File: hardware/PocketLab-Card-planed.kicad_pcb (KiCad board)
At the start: 4 copper layers, 85.6 x 54 mm, 232 parts, among them J1 USB-C DATA/POWER, J2 microSD, J3 GNSS ANT U.FL, J4 PROTECTED 1S LiPo 3.7V, J5 2x15 2.54mm DUPONT EXPANSION, J7 OPTIONAL 10k NTC - CUT SJ1, Q1 AO3400A IR DRIVER, Q2 CSD16406Q3 DISCHARGE, Q3 CSD16406Q3 CHARGE, Q4 AO3400A BUZZER, SW1 RESET, SW2 BOOT, SW3 USER A, SW4 USER B, U1 ESP32-S3-WROOM-1-N8R2, U10 BMI270 (FULL OPTION), U11 BMP390 (FULL OPTION), U12 PCF8563T, U13 TSOP75338WTR 38kHz, U14 BQ29700DSE, U15 TPS2553DBVR 500mA LIMIT, U16 USBLC6-4SC6Y, U17 TPS22919DCKR GNSS LOAD SWITCH, U18 TCA9534PWR INTERNAL CONTROL, U19 SRV05-4MR6T1G SD ESD, U2 PN5321A3HN/C106, U3 E07-900M10S IPEX 868MHz, U4 MAX-M10S-00B, U5 BQ24074RGTR, U6 TPS63070RNMR 3V3, U7 TPS61023DRLR 5V BOOST, U8 MAX17048G+T10, U9 TCA9535PWR, Y301 27.12MHz crystal (pins 2/4 sh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, Y701 32.768kHz CL=7pF

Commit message: Save integrated card hardware and firmware checkpoint
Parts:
- removed BZ1: PKMCS0909E, Buzzer_Beeper:Buzzer_Murata_PKMCS0909E
- removed J7: OPTIONAL 10k NTC - CUT SJ1, Connector_PinHeader_2.54mm:PinHeader_1x02_P2.54mm_Vertical
- removed Q4: AO3400A BUZZER, Package_TO_SOT_SMD:SOT-23
- removed R607: 100k, Resistor_SMD:R_0805_2012Metric
- added A1: T3-868M SPRING ANTENNA, PocketLab_Custom:T3-868M_Edge_Solder, F.Cu at (86.8, 70.5)
- added C403: DNP SUBGHZ MATCH, Capacitor_SMD:C_0805_2012Metric, B.Cu at (75.4, 66.0)
- added C404: DNP SUBGHZ MATCH, Capacitor_SMD:C_0805_2012Metric, B.Cu at (82.8, 66.0)
- added C607: 22uF 10V X5R IR BUFFER, Capacitor_SMD:C_1206_3216Metric, F.Cu at (70.7, 61.5)
- added C608: 100nF IR HF, Capacitor_SMD:C_0805_2012Metric, F.Cu at (64.8, 68.5)
- added C609: 100nF X7R, Capacitor_SMD:C_0805_2012Metric, B.Cu at (65.5, 65.9)
- added C610: 1uF X7R, Capacitor_SMD:C_0805_2012Metric, F.Cu at (83.2, 54.5)
- added C611: 1uF X7R, Capacitor_SMD:C_0805_2012Metric, F.Cu at (83.2, 58.3)
- added C612: 100nF X7R, Capacitor_SMD:C_0805_2012Metric, F.Cu at (80.8, 54.5)
- added C613: 4.7uF X5R, Capacitor_SMD:C_0805_2012Metric, F.Cu at (80.8, 58.3)
- added C614: 2.2uF X7R, Capacitor_SMD:C_0805_2012Metric, F.Cu at (83.2, 62.0)
- added C615: 4.7uF X5R, Capacitor_SMD:C_0805_2012Metric, F.Cu at (80.8, 62.0)
- added C616: 100nF X7R, Capacitor_SMD:C_0805_2012Metric, B.Cu at (81.0, 62.2)
- added C617: 22uF 10V X5R IR BUFFER, Capacitor_SMD:C_1206_3216Metric, B.Cu at (65.0, 62.1)
- added D2: TSAL6200 940nm, PocketLab_Custom:TSAL6200_LayFlat_Inboard, F.Cu at (20.2, 62.2)
- added D3: TSAL6200 940nm, PocketLab_Custom:TSAL6200_LayFlat_Inboard, F.Cu at (20.2, 68.6)
- added J8: ER-OLED0.42-1W 72x40 SSD1306B, PocketLab_Custom:EastRising_ER-OLED0.42-1W_SolderFPC, F.Cu at (90.5, 58.5)
- added J9: GPIO38 2.54mm DUPONT, Connector_PinHeader_2.54mm:PinHeader_1x01_P2.54mm_Vertical, F.Cu at (102.7, 69.5)
- added R405: 0R SUBGHZ MATCH, Resistor_SMD:R_0805_2012Metric, B.Cu at (79.1, 66.0)
- added R610: 39R 0.5W pulse-rated, Resistor_SMD:R_1210_3225Metric, B.Cu at (40.8, 61.8)
- added R611: 39R 0.5W pulse-rated, Resistor_SMD:R_1210_3225Metric, B.Cu at (46.9, 57.5)
- added R735: 100k EN pull-down, Resistor_SMD:R_0805_2012Metric, B.Cu at (85.7, 31.8)
- added SW5: MAIN POWER OFF / ON, Button_Switch_SMD:SW_SPDT_Shouhan_MSK12C02, F.Cu at (92.9, 69.3)
- added U20: SN74AHCT1G126DBVR RGB LEVEL SHIFT, Package_TO_SOT_SMD:SOT-23-5, F.Cu at (65.8, 60.8)
- C501, C502, C603, C604, C605, C606, D501, J3, J4, R501, R502, R505, R608, R609, R710, R711, R712, R715, TP502, TP601: moved to B.Cu
- C510, C511, R401, R402, R403, R404, R510, R511, R512, R513, R730, R731, R732, R733, U19: moved to F.Cu
- D1: footprint LED_THT:LED_D5.0mm -> PocketLab_Custom:TSAL6200_LayFlat_Inboard
- J5: value 2x15 2.54mm DUPONT EXPANSION -> 30-PIN 2.54mm DUPONT GRID; footprint Connector_PinHeader_2.54mm:PinHeader_2x15_P2.54mm_Vertical -> PocketLab_Custom:Dupont_Grid_6x5_P2.54mm
- LED1, LED2, LED3: value WS2812B-MINI-V3 -> WS2812B-2020; footprint LED_SMD:LED_WS2812B-Mini_PLCC4_3.5x3.5mm -> LED_SMD:LED_WS2812B-2020_PLCC4_2.0x2.0mm
- LED4: value WS2812B-MINI-V3 -> WS2812B-2020; footprint LED_SMD:LED_WS2812B-Mini_PLCC4_3.5x3.5mm -> LED_SMD:LED_WS2812B-2020_PLCC4_2.0x2.0mm; moved to F.Cu
- Q2, Q3: footprint Package_SON:VSON-8_3.3x3.3mm_P0.65mm_NexFET -> PocketLab_Custom:CSD16406Q3_VSON-8_3.3x3.3mm_P0.65mm_JLC
- R601: value 39R 1W pulse-rated -> 39R 0.5W pulse-rated; footprint Resistor_SMD:R_2512_6332Metric -> Resistor_SMD:R_1210_3225Metric
- R605: value 330R -> 68R; moved to B.Cu
- R606: value 100R -> 100R GPIO38 PROTECTION; moved to B.Cu
- SW1: footprint Button_Switch_SMD:SW_SPST_TL3305A -> Button_Switch_SMD:SW_Push_1P1T_NO_CK_KMR2
- SW2: footprint Button_Switch_SMD:SW_SPST_TL3305A -> Button_Switch_SMD:SW_Push_1P1T_NO_CK_KMR2; moved to F.Cu
- U1: footprint RF_Module:ESP32-S3-WROOM-1 -> PocketLab_Card:ESP32-S3-WROOM-1_PhysicalCourtyard
- U3: value E07-900M10S IPEX 868MHz -> E07-900MM10S 855-925MHz; footprint PocketLab_Custom:E07-900M10S -> PocketLab_Custom:E07-900MM10S
- moved R128 75.2 mm to (90.6, 32.0)
- moved R513 67.1 mm to (103.1, 42.5), turned to 90 degrees
- moved C605 66.9 mm to (25.7, 21.8), turned to 180 degrees
- moved C606 66.9 mm to (29.7, 21.8), turned to 180 degrees
- moved TP101 66.7 mm to (25.5, 22.3)
- moved U19 66.6 mm to (103.8, 38.5), turned to 90 degrees
- moved TP102 65.8 mm to (28.0, 22.3)
- moved U12 65.5 mm to (42.0, 69.5), turned to 0 degrees
- moved R731 59.6 mm to (82.2, 65.3), turned to 0 degrees
- moved R127 58.6 mm to (90.7, 59.2)
- moved R511 57.2 mm to (87.2, 51.4)
- moved D1 57.1 mm to (20.2, 55.8), turned to 0 degrees
- moved R510 57.0 mm to (81.5, 38.9)
- moved Y701 56.5 mm to (35.5, 69.5), turned to -90 degrees
- moved R605 56.0 mm to (33.7, 21.8), turned to 180 degrees
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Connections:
- net +5V_AUX renamed /+5V_AUX
- net AUX5_EN renamed /AUX5_EN
- net AUX5_FAULT_N renamed /AUX5_FAULT_N
- net BAT_COUT renamed /BAT_COUT
- net BAT_DOUT renamed /BAT_DOUT
- net BAT_FET_MID renamed /BAT_FET_MID
- net BAT_SENSE renamed /BAT_SENSE
- net BAT_VMINUS renamed /BAT_VMINUS
- net BMI_INT1 renamed /BMI_INT1
- net BMI_INT2 renamed /BMI_INT2
- net BMP_INT renamed /BMP_INT
- net BOOST5_EN renamed /BOOST5_EN
- net BOOT_N renamed /BOOT_N
- net BQ_EN1 renamed /BQ_EN1
- net BQ_EN2 renamed /BQ_EN2
- net BUZZER_PWM renamed /GPIO38_MCU
- net CELL_NEG renamed /CELL_NEG
- net CELL_POS renamed /CELL_POS
- net CHARGER_CHG_N renamed /CHARGER_CHG_N
- net CHARGER_PGOOD_N renamed /CHARGER_PGOOD_N
- net CHG_DISABLE renamed /CHG_DISABLE
- net CHG_ILIM renamed /CHG_ILIM
- net CHG_ISET renamed /CHG_ISET
- net CHG_ITERM renamed /CHG_ITERM
- net CHG_TMR renamed /CHG_TMR
- net CHG_TS_FIXED renamed /CHG_TS_FIXED
- net ESP_EN renamed /ESP_EN
- net EX0 renamed /EX0
- net EX0_INT renamed /EX0_INT
- net EX1 renamed /EX1
- net EX1_INT renamed /EX1_INT
- net EX2 renamed /EX2
- net EX2_INT renamed /EX2_INT
- net EX3 renamed /EX3
- net EX3_INT renamed /EX3_INT
- net EX4 renamed /EX4
- net EX4_INT renamed /EX4_INT
- net EX5 renamed /EX5
- net EX5_INT renamed /EX5_INT
- net EX6 renamed /EX6
- net EX6_INT renamed /EX6_INT
- net EX7 renamed /EX7
- net EX7_INT renamed /EX7_INT
- net FG_ALERT_N renamed /FG_ALERT_N
- net GNSS_3V3 renamed /GNSS_3V3
- net GNSS_ANT_FEED renamed /GNSS_ANT_FEED
- net GNSS_BIAS renamed /GNSS_BIAS
- net GNSS_LNA_EN renamed /GNSS_LNA_EN
- net GNSS_POWER_EN renamed /GNSS_POWER_EN
- net GNSS_QOD renamed /GNSS_QOD
- net GNSS_RESET_N renamed /GNSS_RESET_N
- net GNSS_RX_FROM_MODULE renamed /GNSS_RX_FROM_MODULE
- net GNSS_TIMEPULSE renamed /GNSS_TIMEPULSE
- net GNSS_TX_TO_MODULE renamed /GNSS_TX_TO_MODULE
- net GNSS_UART_RX_MOD renamed /GNSS_UART_RX_MOD
- net GNSS_UART_TX_MOD renamed /GNSS_UART_TX_MOD
- net GNSS_VCC_RF renamed /GNSS_VCC_RF
- net GPIO1 renamed /GPIO1
- net GPIO1_MCU renamed /GPIO1_MCU
- net GPIO2 renamed /GPIO2
- net GPIO2_MCU renamed /GPIO2_MCU
- net GPIO4 renamed /GPIO4
- net GPIO40 renamed /GPIO40
- net GPIO40_MCU renamed /GPIO40_MCU
- net GPIO41 renamed /GPIO41
- net GPIO41_MCU renamed /GPIO41_MCU
- net GPIO42 renamed /GPIO42
- net GPIO42_MCU renamed /GPIO42_MCU
- net GPIO43 renamed /GPIO43
- net GPIO43_MCU renamed /GPIO43_MCU
- net GPIO44 renamed /GPIO44
- net GPIO44_MCU renamed /GPIO44_MCU
- net GPIO47 renamed /GPIO47
- net GPIO47_MCU renamed /GPIO47_MCU
- net GPIO48 renamed /GPIO48
- net GPIO48_MCU renamed /GPIO48_MCU
- net GPIO4_MCU renamed /GPIO4_MCU
- net GPIO8 renamed /GPIO8
- net GPIO8_MCU renamed /GPIO8_MCU
- net GPIO9 renamed /GPIO9
- net GPIO9_MCU renamed /GPIO9_MCU
- net I2C_SCL renamed /I2C_SCL
- net I2C_SCL_HDR renamed /I2C_SCL_HDR
- net I2C_SDA renamed /I2C_SDA
- net I2C_SDA_HDR renamed /I2C_SDA_HDR
- net IOEXP_INT_N renamed /IOEXP_INT_N
- net IR_GATE renamed /IR_GATE
- net IR_LED_A renamed /IR_LED_A1
- net IR_LED_K renamed /IR_LED_K
- net IR_RX renamed /IR_RX
- net IR_RX_VS renamed /IR_RX_VS
- net IR_TX renamed /IR_TX
- net JTAG_STRAP_TP renamed /JTAG_STRAP_TP
- net NFC_DVDD renamed /NFC_DVDD
- net NFC_I0 renamed /NFC_I0
- net NFC_IRQ_N renamed /NFC_IRQ_N
- net NFC_LOADMOD renamed /NFC_LOADMOD
- net NFC_LOOP_A renamed /NFC_LOOP_A
- net NFC_LOOP_B renamed /NFC_LOOP_B
- net NFC_OSCIN renamed /NFC_OSCIN
- net NFC_OSCOUT renamed /NFC_OSCOUT
- net NFC_RESET_N renamed /NFC_RESET_N
- net NFC_RX renamed /NFC_RX
- net NFC_RX_AC renamed /NFC_RX_AC
- net NFC_SVDD renamed /NFC_SVDD
- net NFC_TX1 renamed /NFC_TX1
- net NFC_TX1_F renamed /NFC_TX1_F
- net NFC_TX2 renamed /NFC_TX2
- net NFC_TX2_F renamed /NFC_TX2_F
- net NFC_VMID renamed /NFC_VMID
- net PWR_3V3_PG renamed /PWR_3V3_PG
- net RGB_D1_2 renamed /RGB_D1_2
- net RGB_D2_3 renamed /RGB_D2_3
- net RGB_D3_4 renamed /RGB_D3_4
- net RGB_DIN1 renamed /RGB_DIN1
- net RGB_DOUT4 renamed /RGB_DOUT4
- net RTC_OSCI renamed /RTC_OSCI
- net RTC_OSCO renamed /RTC_OSCO
- net SD_CS_DEV renamed /SD_CS_DEV
- net SD_CS_N renamed /SD_CS_N
- net SD_DAT1 renamed /SD_DAT1
- net SD_DAT2 renamed /SD_DAT2
- net SD_DETECT_N renamed /SD_DETECT_N
- net SD_MISO renamed /SD_MISO
- net SD_MOSI renamed /SD_MOSI
- net SD_SCK renamed /SD_SCK
- net SPI_MISO renamed /SPI_MISO
- net SPI_MISO_HDR renamed /SPI_MISO_HDR
- net SPI_MOSI renamed /SPI_MOSI
- net SPI_MOSI_HDR renamed /SPI_MOSI_HDR
- net SPI_SCK renamed /SPI_SCK
- net SPI_SCK_HDR renamed /SPI_SCK_HDR
- net STRAP_BOOT_TP renamed /STRAP_BOOT_TP
- net STRAP_VDD_SPI_TP renamed /STRAP_VDD_SPI_TP
- net SUBGHZ_CS_N renamed /SUBGHZ_CS_N
- net U15_ILIM renamed /U15_ILIM
- net U6_FB renamed /U6_FB
- net U6_L1 renamed /U6_L1
- net U6_L2 renamed /U6_L2
- net U6_VAUX renamed /U6_VAUX
- net U7_FB renamed /U7_FB
- net U7_SW renamed /U7_SW
- net USB_CC1 renamed /USB_CC1
- net USB_CC2 renamed /USB_CC2
- net USB_CONN_N renamed /USB_CONN_N
- net USB_CONN_P renamed /USB_CONN_P
- net USB_D_N renamed /USB_D_N
- net USB_D_P renamed /USB_D_P
- net USB_SHIELD renamed /USB_SHIELD
- net USER_BUTTON_A_N renamed /USER_BUTTON_A_N
- net USER_BUTTON_B_N renamed /USER_BUTTON_B_N
- net VBUS_FUSED renamed /VBUS_FUSED
- net VBUS_USB renamed /VBUS_USB
- C101 pad 2: GND -> /GND
- C103 pad 2: GND -> /GND
- C104 pad 2: GND -> /GND
- C105 pad 1: VSYS -> /VSYS
- C105 pad 2: GND -> /GND
- C106 pad 2: GND -> /GND
- C107 pad 2: GND -> /GND
- C108 pad 1: VSYS -> /VSYS
- C108 pad 2: GND -> /GND
- C109 pad 1: VSYS -> /VSYS
- C109 pad 2: GND -> /GND
- C110 pad 1: +3V3 -> /+3V3
- C110 pad 2: GND -> /GND
- C111 pad 1: +3V3 -> /+3V3
- C111 pad 2: GND -> /GND
- C112 pad 1: +3V3 -> /+3V3
- C112 pad 2: GND -> /GND
- C113 pad 1: +5V_RAW -> /+5V_RAW
- C114 pad 1: VSYS -> /VSYS
- C114 pad 2: GND -> /GND
- C115 pad 1: +5V_RAW -> /+5V_RAW
- C115 pad 2: GND -> /GND
- C116 pad 1: +5V_RAW -> /+5V_RAW
- C116 pad 2: GND -> /GND
- C117 pad 1: +5V_RAW -> /+5V_RAW
- C117 pad 2: GND -> /GND
- C118 pad 2: GND -> /GND
- C119 pad 2: GND -> /GND
- C120 pad 2: GND -> /GND
- C121 pad 2: GND -> /GND
- C122 pad 1: VSYS -> /VSYS
- C122 pad 2: GND -> /GND
- C123 pad 1: VSYS -> /VSYS
- C123 pad 2: GND -> /GND
- C124 pad 1: +3V3 -> /+3V3
- C124 pad 2: GND -> /GND
- C201 pad 2: GND -> /GND
- C202 pad 1: +3V3 -> /+3V3
- C202 pad 2: GND -> /GND
- C203 pad 1: +3V3 -> /+3V3
- C203 pad 2: GND -> /GND
- C301 pad 2: GND -> /GND
- C302 pad 2: GND -> /GND
- C303 pad 1: +3V3 -> /+3V3
- C303 pad 2: GND -> /GND
- C304 pad 2: GND -> /GND
- C305 pad 2: GND -> /GND
- C306 pad 2: GND -> /GND
- C307 pad 2: GND -> /GND
- C308 pad 2: GND -> /GND
- C309 pad 2: GND -> /GND
- C311 pad 2: GND -> /GND
- C312 pad 2: GND -> /GND
- C313 pad 2: GND -> /GND
- C314 pad 2: GND -> /GND
- C315 pad 2: GND -> /GND
- C316 pad 1: +3V3 -> /+3V3
- C316 pad 2: GND -> /GND
- C317 pad 1: +3V3 -> /+3V3
- C317 pad 2: GND -> /GND
- C401 pad 1: +3V3 -> /+3V3
- C401 pad 2: GND -> /GND
- C402 pad 1: +3V3 -> /+3V3
- C402 pad 2: GND -> /GND
- C501 pad 2: GND -> /GND
- C502 pad 2: GND -> /GND
- C504 pad 2: GND -> /GND
- C510 pad 1: +3V3 -> /+3V3
- C510 pad 2: GND -> /GND
- C511 pad 1: +3V3 -> /+3V3
- C511 pad 2: GND -> /GND
- C512 pad 1: +3V3 -> /+3V3
- C512 pad 2: GND -> /GND
- C601 pad 2: GND -> /GND
- C602 pad 2: GND -> /GND
- C603 pad 1: +3V3 -> /+5V_RAW
- C603 pad 2: GND -> /GND
- C604 pad 1: +3V3 -> /+5V_RAW
- C604 pad 2: GND -> /GND
- C605 pad 1: +3V3 -> /+5V_RAW
- C605 pad 2: GND -> /GND
- C606 pad 1: +3V3 -> /+5V_RAW
- C606 pad 2: GND -> /GND
- C701 pad 1: +3V3 -> /+3V3
- C701 pad 2: GND -> /GND
- C702 pad 1: +3V3 -> /+3V3
- C702 pad 2: GND -> /GND
- C703 pad 1: +3V3 -> /+3V3
- C703 pad 2: GND -> /GND
- C704 pad 1: +3V3 -> /+3V3
- C704 pad 2: GND -> /GND
- C705 pad 1: +3V3 -> /+3V3
- C705 pad 2: GND -> /GND
- C706 pad 1: +3V3 -> /+3V3
- C706 pad 2: GND -> /GND
- C707 pad 1: +3V3 -> /+3V3
- C707 pad 2: GND -> /GND
- D101 pad 2: GND -> /GND
- D501 pad 1: GND -> /GND
- J1 pad A1: GND -> /GND
- J1 pad A12: GND -> /GND
- J1 pad B1: GND -> /GND
- J1 pad B12: GND -> /GND
- J2 pad 4: +3V3 -> /+3V3
- J2 pad 6: GND -> /GND
- J2 pad 9: GND -> /GND
- J2 pad SH: GND -> /GND
- J3 pad 2: GND -> /GND
- J5 pad 1: +3V3 -> /+3V3
- J5 pad 2: GND -> /GND
- J5 pad 28: GND -> /CHG_TS
- J5 pad 30: GND -> /GND
- L7 pad 1: VSYS -> /VSYS
- LED1 pad 1: +3V3 -> /+5V_RAW
- LED1 pad 3: GND -> /GND
- LED2 pad 1: +3V3 -> /+5V_RAW
- LED2 pad 3: GND -> /GND
- LED3 pad 1: +3V3 -> /+5V_RAW
- LED3 pad 3: GND -> /GND
- LED4 pad 1: +3V3 -> /+5V_RAW
- LED4 pad 3: GND -> /GND
- Q1 pad 2: GND -> /GND
- Q3 pad 1: GND -> /GND
- Q3 pad 2: GND -> /GND
- Q3 pad 3: GND -> /GND
- R101 pad 2: GND -> /GND
- R102 pad 2: GND -> /GND
- R103 pad 2: GND -> /GND
- R105 pad 2: GND -> /GND
- R107 pad 2: GND -> /GND
- R108 pad 2: GND -> /GND
- R109 pad 2: +3V3 -> /+3V3
- R110 pad 2: +3V3 -> /+3V3
- R111 pad 2: GND -> /GND
- R112 pad 2: GND -> /GND
- R113 pad 2: GND -> /GND
- R114 pad 2: GND -> /GND
- R115 pad 2: GND -> /GND
- R116 pad 1: VSYS -> /VSYS
- R116 pad 2: U6_PS_SYNC -> /PWR_SW_ON
- R117 pad 1: +3V3 -> /+3V3
- R118 pad 2: GND -> /GND
- R119 pad 2: +3V3 -> /+3V3
- R120 pad 1: +5V_RAW -> /+5V_RAW
- R121 pad 2: GND -> /GND
- R122 pad 2: GND -> /GND
- R123 pad 2: GND -> /GND
- R124 pad 2: +3V3 -> /+3V3
- R125 pad 2: +3V3 -> /+3V3
- R126 pad 2: GND -> /GND
- R127 pad 2: GND -> /GND
- R128 pad 2: GND -> /GND
- R203 pad 2: +3V3 -> /+3V3
- R204 pad 2: +3V3 -> /+3V3
- R302 pad 2: GND -> /GND
- R401 pad 2: SUB_SCK -> /SUB_SCK
- R402 pad 2: SUB_MOSI -> /SUB_MOSI
- R403 pad 2: SUB_MISO -> /SUB_MISO
- R404 pad 2: SUB_CS_N -> /SUB_CS_N
- R406 pad 1: SUB_CS_N -> /SUB_CS_N
- R406 pad 2: +3V3 -> /+3V3
- R506 pad 2: GND -> /GND
- R514 pad 2: +3V3 -> /+3V3
- R515 pad 2: +3V3 -> /+3V3
- R516 pad 2: +3V3 -> /+3V3
- R517 pad 2: +3V3 -> /+3V3
- R518 pad 2: +3V3 -> /+3V3
- R519 pad 2: +3V3 -> /+3V3
- R601 pad 1: +5V_RAW -> /+5V_RAW
- R603 pad 2: GND -> /GND
- R604 pad 1: +3V3 -> /+3V3
- R605 pad 1: RGB_DATA -> /RGB_BUF_5V
- R606 pad 2: BUZZER_GATE -> /GPIO38
- R608 pad 2: +3V3 -> /+3V3
- R609 pad 2: +3V3 -> /+3V3
- R701 pad 2: +3V3 -> /+3V3
- R702 pad 2: +3V3 -> /+3V3
- R703 pad 2: +3V3 -> /+3V3
- SJ1 pad 1: CHG_TS -> /CHG_TS
- SW1 pad 2: GND -> /GND
- SW2 pad 2: GND -> /GND
- SW3 pad 2: GND -> /GND
- SW4 pad 2: GND -> /GND
- TP104 pad 1: GND -> /GND
- TP107 pad 1: VSYS -> /VSYS
- TP108 pad 1: +3V3 -> /+3V3
- TP109 pad 1: +5V_RAW -> /+5V_RAW
- U1 pad 1: GND -> /GND
- U1 pad 18: RGB_DATA -> /RGB_DATA
- U1 pad 2: +3V3 -> /+3V3
- U1 pad 40: GND -> /GND
- U1 pad 41: GND -> /GND
- U1 pad 8: SUBGHZ_GDO0 -> /SUBGHZ_GDO0
- U1 pad 9: SUBGHZ_GDO2 -> /SUBGHZ_GDO2
- U10 pad 1: GND -> /GND
- U10 pad 10: (no net) -> unconnected-(U10-Pin_10-Pad10)
- U10 pad 11: (no net) -> unconnected-(U10-Pin_11-Pad11)
- U10 pad 12: +3V3 -> /+3V3
- U10 pad 2: (no net) -> unconnected-(U10-Pin_2-Pad2)
- U10 pad 3: (no net) -> unconnected-(U10-Pin_3-Pad3)
- U10 pad 5: +3V3 -> /+3V3
- U10 pad 6: GND -> /GND
- U10 pad 7: GND -> /GND
- U10 pad 8: +3V3 -> /+3V3
- U11 pad 1: +3V3 -> /+3V3
- U11 pad 10: +3V3 -> /+3V3
- U11 pad 3: GND -> /GND
- U11 pad 5: GND -> /GND
- U11 pad 6: +3V3 -> /+3V3
- U11 pad 8: GND -> /GND
- U11 pad 9: GND -> /GND
- U12 pad 3: (no net) -> unconnected-(U12-~{INT}-Pad3)
- U12 pad 4: GND -> /GND
- U12 pad 7: (no net) -> unconnected-(U12-CLKO-Pad7)
- U12 pad 8: +3V3 -> /+3V3
- U13 pad 1: GND -> /GND
- U13 pad 4: GND -> /GND
- U14 pad 1: (no net) -> unconnected-(U14-NC-Pad1)
- U15 pad 1: +5V_RAW -> /+5V_RAW
- U15 pad 2: GND -> /GND
- U16 pad 2: GND -> /GND
- U17 pad 1: +3V3 -> /+3V3
- U17 pad 2: GND -> /GND
- U17 pad 4: (no net) -> unconnected-(U17-Pin_4-Pad4)
- U18 pad 1: +3V3 -> /+3V3
- U18 pad 16: +3V3 -> /+3V3
- U18 pad 2: GND -> /GND
- U18 pad 3: GND -> /GND
- U18 pad 8: GND -> /GND
- U19 pad 2: GND -> /GND
- U19 pad 5: +3V3 -> /+3V3
- U2 pad 1: GND -> /GND
- U2 pad 11: GND -> /GND
- U2 pad 12: (no net) -> unconnected-(U2-AUX1-Pad12)
- U2 pad 13: (no net) -> unconnected-(U2-AUX2-Pad13)
- U2 pad 17: GND -> /GND
- U2 pad 18: GND -> /GND
- U2 pad 19: (no net) -> unconnected-(U2-P35-Pad19)
- U2 pad 20: (no net) -> unconnected-(U2-N.C.-Pad20)
- U2 pad 21: (no net) -> unconnected-(U2-N.C.-Pad21)
- U2 pad 22: (no net) -> unconnected-(U2-N.C.-Pad22)
- U2 pad 23: +3V3 -> /+3V3
- U2 pad 24: (no net) -> unconnected-(U2-P30/UART_RX-Pad24)
- U2 pad 26: (no net) -> unconnected-(U2-~{RSTOUT}-Pad26)
- U2 pad 29: (no net) -> unconnected-(U2-MISO/P71-Pad29)
- U2 pad 3: GND -> /GND
- U2 pad 30: (no net) -> unconnected-(U2-SCK/P72-Pad30)
- U2 pad 31: (no net) -> unconnected-(U2-P31/UART_TX-Pad31)
- U2 pad 32: (no net) -> unconnected-(U2-P32_INT0-Pad32)
- U2 pad 33: (no net) -> unconnected-(U2-P33_INT1-Pad33)
- U2 pad 34: (no net) -> unconnected-(U2-SIC_CLK/P34-Pad34)
- U2 pad 35: (no net) -> unconnected-(U2-SIGOUT-Pad35)
- U2 pad 36: (no net) -> unconnected-(U2-SIGIN-Pad36)
- U2 pad 40: +3V3 -> /+3V3
- U2 pad 41: GND -> /GND
- U2 pad 7: GND -> /GND
- U3 pad 1: GND -> /+3V3
- U3 pad 10: (no net) -> unconnected-(U3-Pin_10-Pad10)
- U3 pad 11: GND -> unconnected-(U3-Pin_11-Pad11)
- U3 pad 12: GND -> /SUB_MISO
- U3 pad 13: (no net) -> /SUB_MOSI
- U3 pad 14: SUBGHZ_GDO2 -> /SUB_CS_N
- U3 pad 15: SUBGHZ_GDO0 -> /SUB_SCK
- U3 pad 16: SUB_MISO -> /GND
- U3 pad 17: SUB_MOSI -> unconnected-(U3-Pin_17-Pad17)
- U3 pad 18: SUB_SCK -> /SUBGHZ_GDO0
- U3 pad 19: SUB_CS_N -> unconnected-(U3-Pin_19-Pad19)
- U3 pad 2: GND -> /GND
- U3 pad 20: GND -> /SUBGHZ_GDO2
- U3 pad 3: GND -> unconnected-(U3-Pin_3-Pad3)
- U3 pad 4: GND -> unconnected-(U3-Pin_4-Pad4)
- U3 pad 5: GND -> unconnected-(U3-Pin_5-Pad5)
- U3 pad 6: (no net) -> /SUBGHZ_RF_MOD
- U3 pad 7: (no net) -> /GND
- U3 pad 8: (no net) -> unconnected-(U3-Pin_8-Pad8)
- U3 pad 9: +3V3 -> unconnected-(U3-Pin_9-Pad9)
- U4 pad 1: GND -> /GND
- U4 pad 10: GND -> /GND
- U4 pad 12: GND -> /GND
- U4 pad 15: (no net) -> unconnected-(U4-VIO_SEL-Pad15)
- U4 pad 16: (no net) -> unconnected-(U4-SDA-Pad16)
- U4 pad 17: (no net) -> unconnected-(U4-SCL-Pad17)
- U4 pad 18: (no net) -> unconnected-(U4-~{SAFEBOOT}-Pad18)
- U4 pad 5: (no net) -> unconnected-(U4-EXTINT-Pad5)
- U4 pad 6: (no net) -> unconnected-(U4-V_BCKP-Pad6)
- U5 pad 1: CHG_TS -> /CHG_TS
- U5 pad 10: VSYS -> /VSYS
- U5 pad 11: VSYS -> /VSYS
- U5 pad 17: GND -> /GND
- U5 pad 8: GND -> /GND
- U6 pad 1: U6_PS_SYNC -> /U6_PS_SYNC
- U6 pad 10: GND -> /GND
- U6 pad 12: VSYS -> /VSYS
- U6 pad 13: VSYS -> /VSYS
- U6 pad 14: VSYS -> /U6_PS_SYNC
- U6 pad 15: GND -> /GND
- U6 pad 4: GND -> /GND
- U6 pad 6: (no net) -> unconnected-(U6-Pin_6-Pad6)
- U6 pad 7: +3V3 -> /+3V3
- U6 pad 8: +3V3 -> /+3V3
- U7 pad 3: VSYS -> /VSYS
- U7 pad 4: GND -> /GND
- U7 pad 6: +5V_RAW -> /+5V_RAW
- U8 pad 1: GND -> /GND
- U8 pad 2: (no net) -> unconnected-(U8-Pin_2-Pad2)
- U8 pad 4: GND -> /GND
- U8 pad 6: GND -> /GND
- U8 pad 9: GND -> /GND
- U9 pad 12: GND -> /GND
- U9 pad 2: GND -> /GND
- U9 pad 21: GND -> /GND
- U9 pad 24: +3V3 -> /+3V3
- U9 pad 3: GND -> /GND
- Y301 pad 2: GND -> /GND
- Y301 pad 4: GND -> /GND
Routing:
- added copper zone on In2.Cu, net /+3V3
- added copper zone on In1.Cu, net /GND
- removed copper zone on In2.Cu, net +3V3
- removed copper zone on In1.Cu, net GND
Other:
- outline, holes or cut-outs redrawn
- board text added: "+"
- board text added: "-"
- board text added: "868MHz SPRING INSIDE POCKET"
- board text added: "BOOT"
- board text added: "RESET"

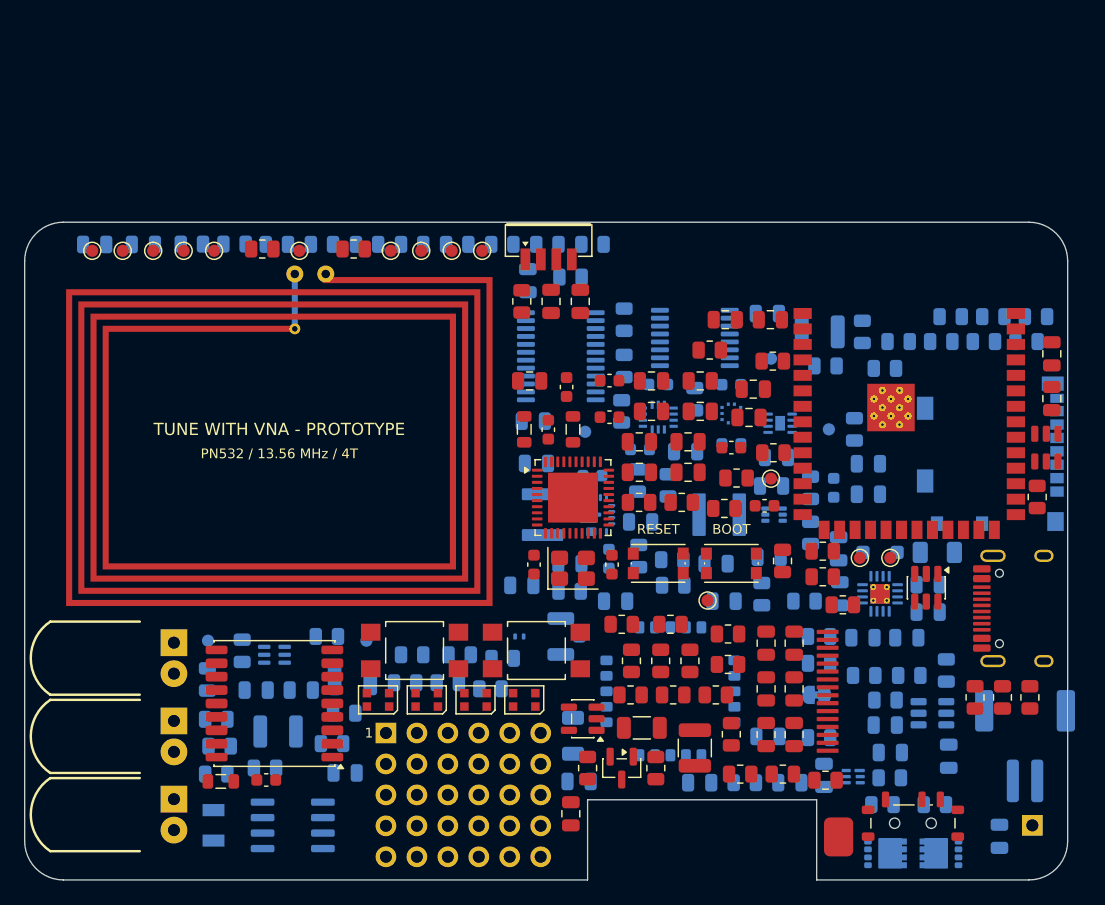
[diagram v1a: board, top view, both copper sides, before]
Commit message: Save RFID and critical routing checkpoint
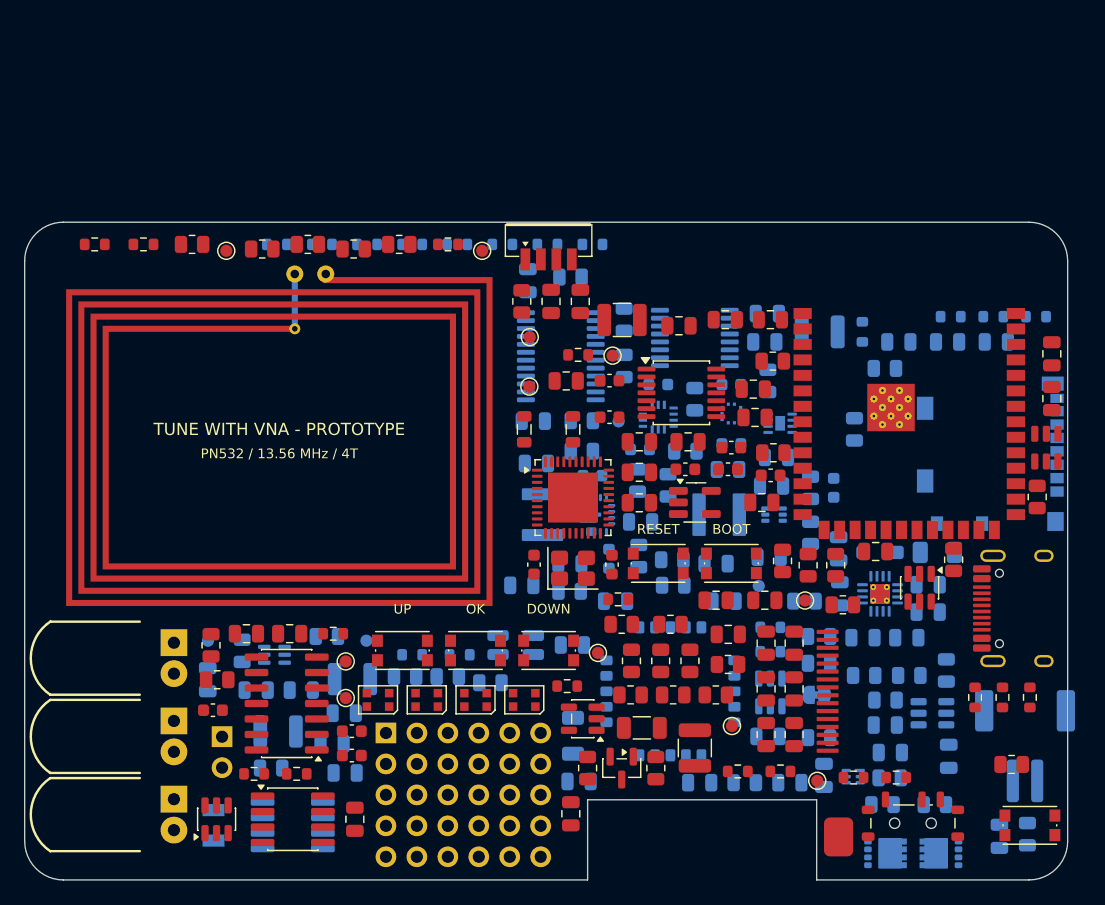
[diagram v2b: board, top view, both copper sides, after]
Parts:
- removed D501: TPD1E0B04 0.13pF RF ESD, Package_SON:Texas_DPY0002A_0.6x1mm_P0.65mm
- removed J9: GPIO38 2.54mm DUPONT, Connector_PinHeader_2.54mm:PinHeader_1x01_P2.54mm_Vertical
- removed L501: 27nH high-Q DNP ACTIVE-ANT BIAS, Inductor_SMD:L_0805_2012Metric
- removed R505: 10R 0.25W DNP ACTIVE-ANT BIAS, Resistor_SMD:R_0805_2012Metric
- removed R507, R508: 1k UART BACKPOWER LIMIT, Resistor_SMD:R_0805_2012Metric
- removed TP601: RGB DOUT, TestPoint:TestPoint_Pad_D1.0mm
- removed TP701: BMI INT1, TestPoint:TestPoint_Pad_D1.0mm
- removed TP702: BMP INT, TestPoint:TestPoint_Pad_D1.0mm
- removed TP703: BMI INT2, TestPoint:TestPoint_Pad_D1.0mm
- added C503: 100nF CEXT, Capacitor_SMD:C_0805_2012Metric, F.Cu at (38.2, 53.8)
- added C505: 100nF C0G COIL ISOLATION, Capacitor_SMD:C_0805_2012Metric, B.Cu at (46.2, 60.3)
- added C506: 3.9nF C0G LF RESONANCE, Capacitor_SMD:C_0805_2012Metric, B.Cu at (45.2, 62.8)
- added C507: 100pF C0G DNP LF TUNE, Capacitor_SMD:C_0603_1608Metric, F.Cu at (46.9, 61.8)
- added C508: 220pF C0G DNP LF TUNE, Capacitor_SMD:C_0603_1608Metric, F.Cu at (46.9, 63.8)
- added C509: 10pF C0G DNP RX EMI, Capacitor_SMD:C_0603_1608Metric, F.Cu at (35.5, 60.0)
- added C513: 100nF OSC supply, Capacitor_SMD:C_0805_2012Metric, B.Cu at (65.0, 54.7)
- added C515: 100nF AHCT supply, Capacitor_SMD:C_0805_2012Metric, F.Cu at (73.7, 28.5)
- added C516: 100nF LVC supply, Capacitor_SMD:C_0805_2012Metric, F.Cu at (80.5, 43.0)
- added C517: 100nF secure element, Capacitor_SMD:C_0805_2012Metric, F.Cu at (47.1, 69.0)
- added R503: 1k LF EMI RETURN, Resistor_SMD:R_0805_2012Metric, B.Cu at (40.2, 64.8)
- added R504: 150k 1% RX DIVIDER, Resistor_SMD:R_0805_2012Metric, F.Cu at (35.8, 57.5)
- added R509: 10k PAIR pull-up, Resistor_SMD:R_0805_2012Metric, F.Cu at (101.0, 64.5)
- added R607: 10k, Resistor_SMD:R_0603_1608Metric, F.Cu at (68.7, 51.0)
- added R736: 10k 1% BOARD TEMP BIAS, Resistor_SMD:R_0603_1608Metric, B.Cu at (81.2, 53.2)
- added RT701: 10k NTC B3950 1%, Resistor_SMD:R_0603_1608Metric, B.Cu at (81.2, 55.2)
- added SW6: PAIR, Button_Switch_SMD:SW_Push_1P1T_NO_CK_KMR2, F.Cu at (102.5, 69.5)
- added SW7: SELECT, Button_Switch_SMD:SW_Push_1P1T_NO_CK_KMR2, F.Cu at (57.0, 55.1)
- added U21: SN74AHCT125PWR LF 3V3-TO-5V, Package_SO:TSSOP-14_4.4x5mm_P0.65mm, F.Cu at (73.9, 34.0)
- added U22: SN74LVC1G17DBVR LF 5V-TO-3V3, Package_TO_SOT_SMD:SOT-23-5_HandSoldering, F.Cu at (75.0, 43.0)
- added U23: ATECC608C-SSHDA-T, Package_SO:SOIC-8_3.9x4.9mm_P1.27mm, F.Cu at (42.0, 69.0)
- added U24: SRV05-4MR6T1G J5 BUS ESD, Package_TO_SOT_SMD:SOT-23-6, F.Cu at (35.8, 69.0)
- added U25: SRV05-4MR6T1G J5 SPI ESD, Package_TO_SOT_SMD:SOT-23-6, B.Cu at (81.2, 58.6)
- added Y501: 4MHz 5V CMOS OSCILLATOR, Oscillator:Oscillator_SMD_EuroQuartz_XO32-4Pin_3.2x2.5mm_RotB_HandSoldering, B.Cu at (60.3, 54.7)
- C501: value 100nF -> 100nF HTRC supply
- C502: value 10uF -> 10uF HTRC pulse reservoir
- C504: value 10nF DNP ACTIVE-ANT BIAS -> 100nF QGND; footprint Capacitor_SMD:C_0603_1608Metric -> Capacitor_SMD:C_0805_2012Metric
- J3: value GNSS ANT U.FL -> EXTERNAL 400uH LF COIL; footprint Connector_Coaxial:U.FL_Hirose_U.FL-R-SMT-1_Vertical -> Connector_PinHeader_2.54mm:PinHeader_1x02_P2.54mm_Vertical
- R102, R517, R518, R519, R610: moved to F.Cu
- R502: value 10k -> 47R 0.5W ANTENNA CURRENT LIMIT; footprint Resistor_SMD:R_0805_2012Metric -> Resistor_SMD:R_1210_3225Metric
- R605, R734: footprint Resistor_SMD:R_0805_2012Metric -> Resistor_SMD:R_0603_1608Metric; moved to F.Cu
- R606: value 100R GPIO38 PROTECTION -> 100R PAIR GPIO PROTECTION; footprint Resistor_SMD:R_0805_2012Metric -> Resistor_SMD:R_0603_1608Metric; moved to F.Cu
- R608, R609, R710, R711, R712, R713, R715, R716, R717, R718, R719, R720, R721, R722, R723, R724, R725, R726, R727, R728, R729, R730, R731, R732, R733: footprint Resistor_SMD:R_0805_2012Metric -> Resistor_SMD:R_0603_1608Metric
- R714: value 100R -> 100R BOARD TEMP PROBE; footprint Resistor_SMD:R_0805_2012Metric -> Resistor_SMD:R_0603_1608Metric
- SW3: value USER A -> UP; footprint Button_Switch_SMD:SW_SPST_TL3305A -> Button_Switch_SMD:SW_Push_1P1T_NO_CK_KMR2
- SW4: value USER B -> DOWN; footprint Button_Switch_SMD:SW_SPST_TL3305A -> Button_Switch_SMD:SW_Push_1P1T_NO_CK_KMR2
- TP107, TP108, TP109, TP110: moved to B.Cu
- TP502: value LNA ENABLE -> LF ANTENNA TAP - HIGH VOLTAGE; moved to F.Cu
- U17: value TPS22919DCKR GNSS LOAD SWITCH -> TPS22919DCKR LF 5V LOAD SWITCH
- U4: value MAX-M10S-00B -> HTRC11001T/03EE,11 125kHz; footprint RF_GPS:ublox_MAX -> Package_SO:SO-14_3.9x8.65mm_P1.27mm
- moved C605 70.5 mm to (95.7, 29.8)
- moved C606 70.5 mm to (99.7, 29.8)
- moved R605 69.8 mm to (88.0, 65.6), turned to 0 degrees
- moved R606 69.8 mm to (91.5, 65.6), turned to 0 degrees
- moved TP104 67.8 mm to (85.0, 65.8)
- moved TP103 61.5 mm to (78.0, 61.3)
- moved R713 61.0 mm to (25.8, 21.8)
- moved R714 59.1 mm to (29.8, 21.8)
- moved C603 57.0 mm to (35.0, 57.5), turned to 90 degrees
- moved TP102 51.1 mm to (67.0, 55.3)
- moved R734 47.6 mm to (82.0, 65.1), turned to 0 degrees
- moved R204 47.6 mm to (35.3, 54.7), turned to 90 degrees
- moved R519 46.0 mm to (50.7, 21.8), turned to 0 degrees
- moved R610 44.0 mm to (69.0, 28.0), turned to 0 degrees
- moved R518 43.1 mm to (43.2, 21.8), turned to 0 degrees
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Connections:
- net /GNSS_POWER_EN renamed /LF_RFID_EN
- net /GNSS_QOD renamed /LF_QOD
- net /GPIO9 renamed /BOARD_TEMP_HDR
- net /GPIO9_MCU renamed /BOARD_TEMP_ADC
- C501 pad 1: /GNSS_3V3 -> /LF_5V
- C502 pad 1: /GNSS_3V3 -> /LF_5V
- C504 pad 1: /GNSS_BIAS -> /LF_QGND
- J3 pad 1: /GNSS_ANT_FEED -> /LF_ANT_A
- J3 pad 2: /GND -> /LF_ANT_B
- LED4 pad 2: /RGB_DOUT4 -> unconnected-(LED4-DOUT-Pad2)
- R501 pad 2: /GNSS_3V3 -> /LF_5V
- R502 pad 1: /GNSS_RESET_N -> /LF_ANT_B
- R502 pad 2: /GNSS_3V3 -> /LF_TAP
- R606 pad 2: /GPIO38 -> /PAIR_N
- TP502 pad 1: /GNSS_LNA_EN -> /LF_TAP
- U1 pad 11: /GNSS_TIMEPULSE -> /LF_SCLK_3V3
- U1 pad 23: /GNSS_RX_FROM_MODULE -> /LF_DOUT_3V3
- U1 pad 28: /GNSS_TX_TO_MODULE -> /LF_DIN_3V3
- U11 pad 7: /BMP_INT -> unconnected-(U11-Pin_7-Pad7)
- U17 pad 1: /+3V3 -> /+5V_RAW
- U17 pad 6: /GNSS_3V3 -> /LF_5V
- U4 pad 10: /GND -> /LF_DOUT_5V
- U4 pad 11: /GNSS_ANT_FEED -> (no net)
- U4 pad 12: /GND -> /LF_CEXT
- U4 pad 13: /GNSS_LNA_EN -> /LF_QGND
- U4 pad 14: /GNSS_VCC_RF -> /LF_RX
- U4 pad 2: /GNSS_UART_TX_MOD -> /LF_TX2
- U4 pad 3: /GNSS_UART_RX_MOD -> /LF_5V
- U4 pad 4: /GNSS_TIMEPULSE -> /LF_TX1
- U4 pad 5: unconnected-(U4-EXTINT-Pad5) -> /GND
- U4 pad 6: unconnected-(U4-V_BCKP-Pad6) -> /LF_CLK_4M
- U4 pad 7: /GNSS_3V3 -> unconnected-(U4-XTAL2-Pad7)
- U4 pad 8: /GNSS_3V3 -> /LF_SCLK_5V
- U4 pad 9: /GNSS_RESET_N -> /LF_DIN_5V
- U9 pad 11: /BMP_INT -> /USER_BUTTON_SELECT_N
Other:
- board text added: "DOWN"
- board text added: "OK"
- board text added: "UP"
